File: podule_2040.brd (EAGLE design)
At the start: 100 x 79.8 mm, 58 parts, among them IC1 LT1963EST-3.3, IC2 RP2040-QFN56, IC3 SN74ALVC164245, IC4 SN74ALVC164245, U1 W25Q32FV, Y1 12MHz

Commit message: Schematic & board V1: as used for prototype fab
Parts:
- added C1: 0.1uF, rcl:C0603K
- added R12: 100K, rcl:R0805
- added RESET: Tact sw, SparkFun-Switches:TACTILE_SWITCH_SMD_5.2MM
- GPIO: device SparkFun-Connectors:1X05 -> matt:1X05
- J2: device SparkFun-Connectors:USB-B-MICRO-SMD -> SparkFun-Connectors:USB-MICROB
- LED1: device led:CHIPLED_0805 -> led:CHIPLED_1206
- SWD: device SparkFun-Connectors:1X04 -> matt:1X04
- moved BOOT 8.98 mm to (7.62, 69.8), turned to 90 degrees
- moved BOOTSEL 6.48 mm to (17.8, 74.9), turned to 90 degrees
- moved GPIO 5.08 mm to (62.2, 69.8)
- moved SWD 3.86 mm to (92.7, 49.5)
- moved R3 1.80 mm to (25.4, 67.3)
- moved R11 0.32 mm to (54.3, 73.7)
- moved J2 0.32 mm to (39.7, 78.1), turned to 90 degrees
- turned C12 to 270 degrees
- turned C14 to 270 degrees
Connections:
- removed net N$14: IC2.26, SWD.4
- new net RUN: C1.1, IC2.26, R12.1, RESET.3, SWD.4
- net +3V3: now also R12.2
- net GND: now also C1.2, J2.MT1, J2.MT2, J2.P$1, J2.P$2, RESET.1; no longer J2.SHIELD1, J2.SHIELD2, J2.SHIELD3
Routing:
- net RUN: track 0.00 -> 160.5 mm, vias 0 -> 3
- net N$14: track 43.3 -> 0.00 mm, vias 2 -> 0
- net GND: track 706.3 -> 721.2 mm, vias 43 -> 56
- net +3V3: track 278.9 -> 288.7 mm
- net N$12: track 13.6 -> 21.7 mm
- net +5V: track 173.6 -> 169.8 mm
- net N$11: track 30.2 -> 28.9 mm
- net N$26: track 3.42 -> 4.23 mm
- net N$16: track 44.7 -> 45.3 mm
- net N$15: track 43.2 -> 43.8 mm
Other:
- board text added: "Arc Pipe Podule (c) 2021 Matt Evans v1 31 Aug 2021"
- board text removed: "Arc Pipe Podule (c) 2021 Matt Evans v0.1 23 Aug 2021"

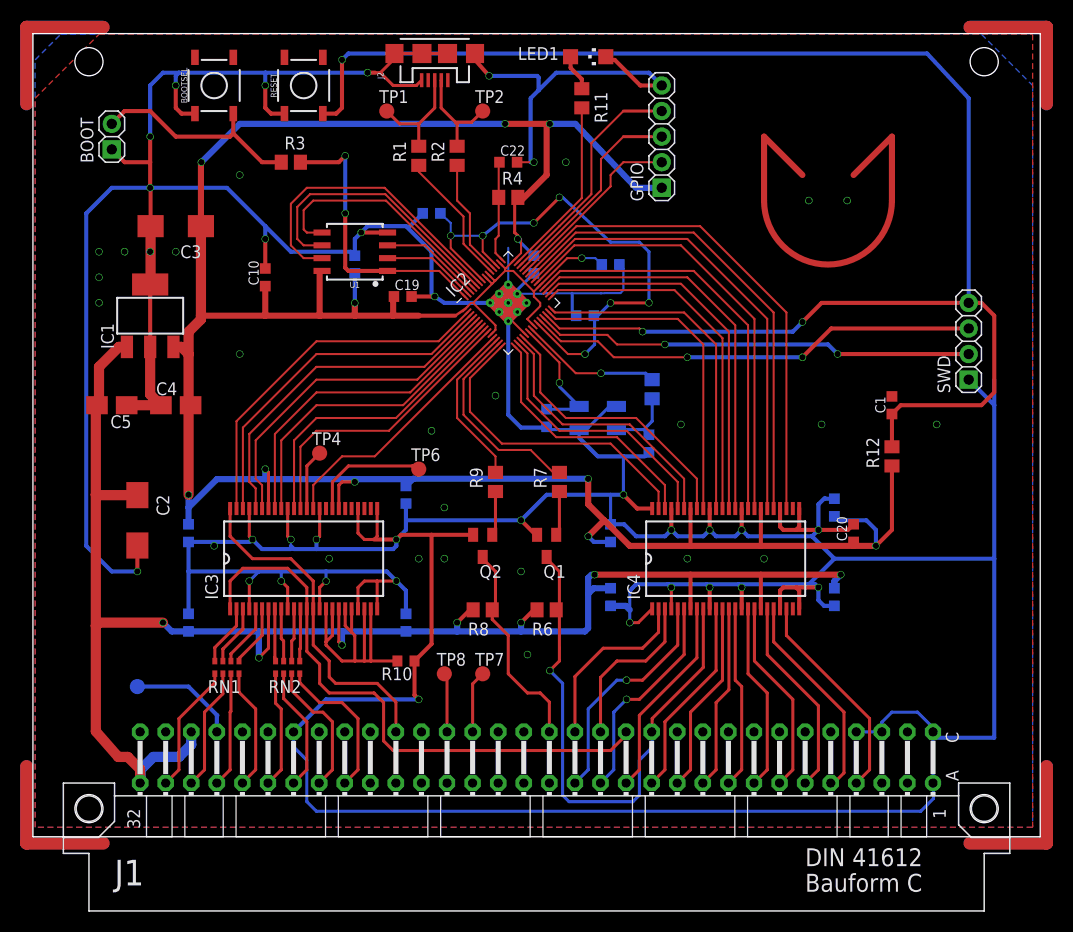
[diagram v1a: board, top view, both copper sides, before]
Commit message: First commit of v2 design, for checking
Changes include:
- Shrink buffers to TSSOP
- Term. resistor packs on internal signals
- Removed N_RST input, freeing 4 GPIOs
- GPIOs to header, prototyping area, and added uSD footprint/resistors
- Moved QSPI closer, more decoupling, re-routed
- Brought reset/boot to a header for remote reboot
- Better labelling/silkscreen tidy, space for serial number
- More common LDO footprint
- Different crystal footprint
- Address lines contiguous
- USB VBUS can power the board, via diodes
- Flash /CS pullup footprint
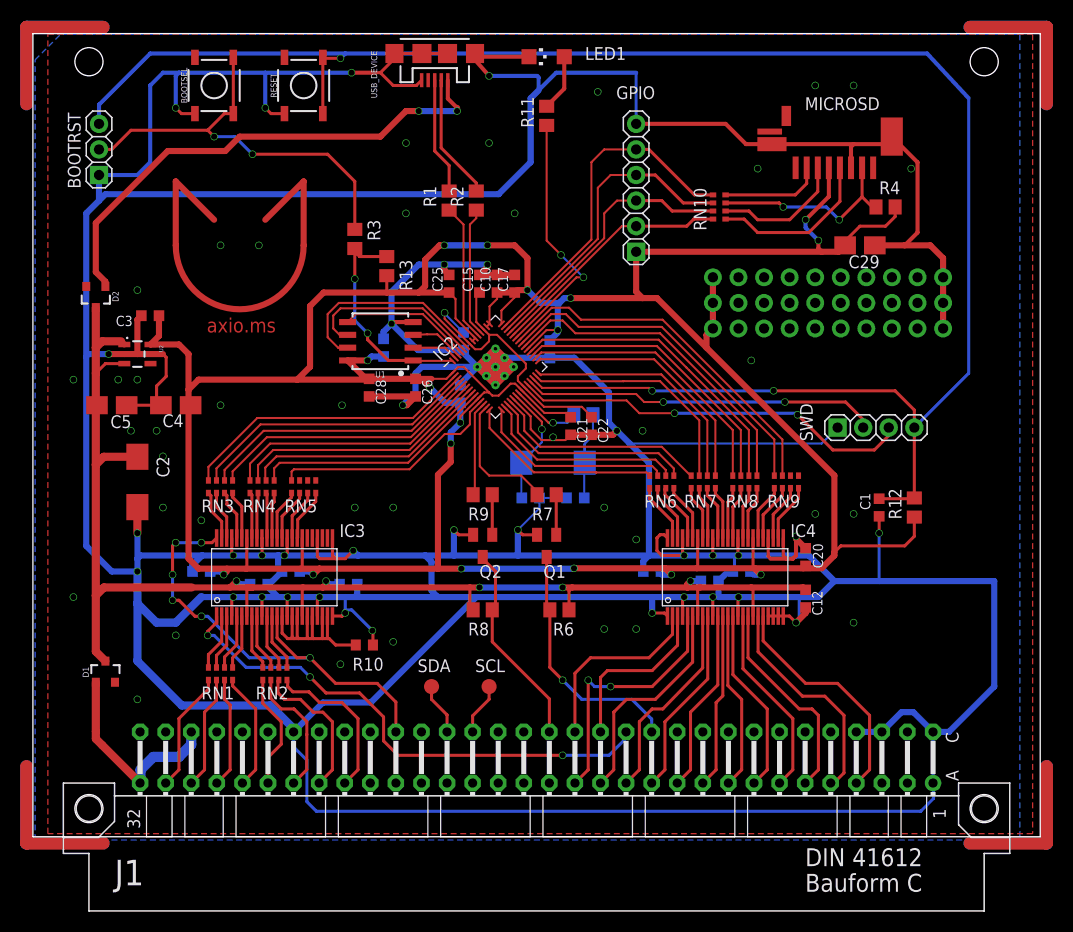
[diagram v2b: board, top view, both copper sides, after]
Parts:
- removed BOOT: (no value), matt:1X02
- removed IC1: LT1963EST-3.3, linear-technology:SOT223
- removed TP1, TP2, TP3, TP4, TP6, TP7, TP8: TPTP15R, testpad:TP15R
- removed Y1: 12MHz, SparkFun-Clocks:CRYSTAL-SMD-5X3.2-4PAD
- added BOOTRST: (no value), matt:1X03
- added C25, C26, C28: 0.1uF, rcl:C0603K
- added C27: 1uF, rcl:C0603K
- added C29: 10uF, rcl:A/3216-18W
- added D1, D2: 700mA/40V/533mV, SparkFun-DiscreteSemi:SOT23-3
- added MICROSD: MOLEX-USD-47309, matt:MOLEX-USD-47309
- added R13: 10K, rcl:R0805
- added RN10: 0, resistor-dil:0603-ARC
- added RN3, RN4, RN5, RN6, RN7, RN8, RN9: 33, resistor-dil:0603-ARC
- added SCL, SDA: TPTP15R, testpad:TP15R
- added U2: 3.3V/150mA, SparkFun-IC-Power:SOT23-5
- added X1: 12MHz, 18pF, IQD-Frequency-Products:7.5X5-2-PAD
- C10: value 0.1uF -> 1uF
- C15: value 2.2uF -> 1uF
- C17, C22: value 2.2uF -> 0.1uF
- C23, C24: value 15pF -> 27pF
- C3: value 100uF -> 1uF; device rcl:CT6032 -> rcl:C0603K
- GPIO: device matt:1X05 -> matt:1X06
- IC3, IC4: value SN74ALVC164245 -> SN74ALVC164245TSSOP48; device matt:DL_R-PDSO-G48 -> matt:TSSOP48
- Q1, Q2: value (none) -> NPN BJT
- R4: value 220 -> 10K
- moved R4 37.5 mm to (84.5, 62.9)
- moved C22 27.5 mm to (55.2, 41.1), turned to 270 degrees
- moved C21 26.8 mm to (53.2, 41.1), flipped to the top, turned to 270 degrees
- moved C10 23.0 mm to (45.9, 55.2)
- moved C6 13.7 mm to (25.4, 26.7), turned to 0 degrees
- moved C16 13.1 mm to (42.5, 49.5), turned to 270 degrees
- moved SWD 12.6 mm to (83.5, 41.0), turned to 0 degrees
- moved C19 11.2 mm to (42.2, 44.3), flipped to the bottom, turned to 90 degrees
- moved C7 11.2 mm to (70.2, 26.7), turned to 0 degrees
- moved C15 10.9 mm to (44.1, 55.2), flipped to the top, turned to 90 degrees
- moved C18 10.4 mm to (51.1, 48.7), turned to 270 degrees
- moved C1 10.2 mm to (83.8, 33.0), turned to 270 degrees
- moved C14 9.97 mm to (67.0, 25.7), turned to 180 degrees
- moved R3 9.92 mm to (31.8, 59.7), turned to 270 degrees
- moved C3 9.25 mm to (11.4, 52.1)
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- renumbered J2 to USB_DEVICE
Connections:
- removed net +12V: J1.C32
- removed net -5V: J1.C2
- removed net N$25: GPIO.4, IC2.40
- removed net NRST_I: IC2.27, IC4.40
- removed net REF8M: J1.C29, TP3.TP
- removed net VBUS: USB_DEVICE.VBUS
- new net +5V/1: D1.1, J1.A32, J1.C30
- new net N$14: MICROSD.2, RN10.8
- new net N$27: IC3.46, RN3.2
- new net N$30: IC3.44, RN3.3
- new net N$31: IC3.43, RN3.4
- new net N$32: IC3.40, RN4.2
- new net N$33: IC3.41, RN4.1
- new net N$34: IC3.38, RN4.3
- new net N$35: IC3.37, RN4.4
- new net N$36: IC3.36, RN5.1
- new net N$37: IC3.35, RN5.2
- new net N$38: IC3.33, RN5.3
- new net N$39: IC4.47, RN6.1
- new net N$40: IC4.46, RN6.2
- new net N$41: IC4.44, RN6.3
- new net N$42: IC4.43, RN6.4
- new net N$43: IC4.41, RN7.1
- new net N$44: IC4.40, RN7.2
- new net N$45: IC4.38, RN7.3
- new net N$46: IC4.37, RN7.4
- new net N$47: IC4.36, RN8.1
- new net N$48: IC4.35, RN8.2
- new net N$49: IC4.33, RN8.3
- new net N$50: IC4.32, RN8.4
- new net N$51: IC4.30, RN9.1
- new net N$52: IC4.29, RN9.2
- new net N$53: IC4.27, RN9.3
- new net N$54: IC4.26, RN9.4
- new net SPI_CS: GPIO.5, IC2.41, RN10.1
- new net SPI_RX: GPIO.4, IC2.40, RN10.2
- new net SPI_SCK: GPIO.2, IC2.38, RN10.4
- new net SPI_TX: GPIO.3, IC2.39, RN10.3
- new net V_USB: D2.1, USB_DEVICE.VBUS
- net +3V3: now also C25.1, C26.1, C27.1, C28.1, C29.+, C3.1, IC2.43, MICROSD.4, R13.2, U2.5; no longer C3.+, IC1.3
- net +5V: now also D1.3, D2.3, U2.1, U2.3; no longer IC1.1, J1.A32, J1.C30
- net A10: now also IC2.32, RN8.6; no longer IC2.34, IC4.32
- net A11: now also IC2.34, RN8.5; no longer IC2.35, IC4.30
- net A12: now also IC2.35, RN9.8; no longer IC2.36, IC4.29
- net A13: now also IC2.36, RN9.7; no longer IC2.37, IC4.27
- net A2: now also RN6.6; no longer IC4.44
- net A3: now also RN6.5; no longer IC4.43
- net A4: now also RN7.8; no longer IC4.41
- net A5: now also IC2.27, RN7.7; no longer IC2.28, IC4.38
- net A6: now also IC2.28, RN7.6; no longer IC2.29, IC4.37
- net A7: now also IC2.29, RN7.5; no longer IC2.30, IC4.36
- net A8: now also IC2.30, RN8.8; no longer IC2.31, IC4.35
- net A9: now also IC2.31, RN8.7; no longer IC2.32, IC4.33
- net D0: now also RN3.8; no longer IC3.47
- net D1: now also RN3.7; no longer IC3.46
- net D2: now also RN3.6; no longer IC3.44
- net D3: now also RN3.5; no longer IC3.43
- net D4: now also RN4.8; no longer IC3.41
- net D5: now also RN4.7; no longer IC3.40
- net D6: now also RN4.6; no longer IC3.38
- net D7: now also RN4.5; no longer IC3.37
- net GND: now also BOOTRST.1, BOOTSEL.2, C25.2, C26.2, C27.2, C28.2, C29.-, C3.2, GPIO.6, IC4.22, IC4.23, MICROSD.6, MICROSD.G1, MICROSD.G2, RESET.2, U2.2; no longer BOOT.1, C3.-, GPIO.5, IC1.2, IC1.4, Y1.2, Y1.4
- net LA10: now also IC4.16; no longer IC4.17
- net LA11: now also IC4.17; no longer IC4.19
- net LA12: now also IC4.19; no longer IC4.20
- net LA13: now also IC4.20; no longer IC4.22
- net LA5: now also IC4.9; no longer IC4.11
- net LA6: now also IC4.11; no longer IC4.12
- net LA7: now also IC4.12; no longer IC4.13
- net LA8: now also IC4.13; no longer IC4.14
- net LA9: now also IC4.14; no longer IC4.16
- net N$10: now also MICROSD.5, RN10.5; no longer C22.1, IC2.43, R4.1
- net N$11: now also R13.1
- net N$12: now also BOOTRST.2, BOOTSEL.4; no longer BOOT.2
- net N$17: now also X1.2; no longer Y1.1
- net N$19: now also X1.1; no longer Y1.3
- net N$21: now also IC3.47, RN3.1; no longer IC3.36, TP4.TP
- net N$22: now also IC3.14
- net N$23: now also MICROSD.3, RN10.6; no longer GPIO.2, IC2.38
- net N$24: now also MICROSD.7, R4.1, RN10.7; no longer GPIO.3, IC2.39
- net N$28: now also IC2.37; no longer IC2.41
- net N$29: now also RN5.4; no longer TP6.TP
- net N$3: no longer TP1.TP
- net N$4: no longer TP2.TP
- net NPS: now also IC3.13; no longer IC3.14
- net NRD: now also RN6.8; no longer IC4.47
- net NRST: no longer IC4.9
- net NSEL: now also RN5.8; no longer IC3.35
- net NWR: now also RN6.7; no longer IC4.46
- net PRNW: no longer IC3.13
- net RUN: now also BOOTRST.3, RESET.4
- net SCL: now also SCL.TP; no longer TP7.TP
- net SDA: now also SDA.TP; no longer TP8.TP
- net VCCINT: now also C22.1
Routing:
- net GND: track 721.2 -> 827.1 mm, vias 56 -> 76
- net +3V3: track 288.7 -> 364.1 mm, vias 12 -> 20
- net V_USB: track 0.00 -> 50.6 mm, vias 0 -> 2
- net SPI_CS: track 0.00 -> 34.4 mm
- net NRST_I: track 33.0 -> 0.00 mm
- net SPI_RX: track 0.00 -> 30.9 mm
- net NRST: track 54.9 -> 24.8 mm
- net +5V: track 169.8 -> 140.7 mm, vias 7 -> 5
- net SPI_TX: track 0.00 -> 27.5 mm
- net VCCINT: track 56.6 -> 30.5 mm, vias 7 -> 1
- net RUN: track 160.5 -> 186.4 mm
- net SPI_SCK: track 0.00 -> 24.7 mm
- net N$25: track 23.4 -> 0.00 mm, vias 0 -> 3
- net +5V/1: track 0.00 -> 20.5 mm
- net N$12: track 21.7 -> 41.9 mm, vias 0 -> 2
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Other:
- board text added: "3.3V"
- board text added: "Arc Pipe Podule (c) 2021 Matt Evans"
- board text added: "Boot"
- board text added: "Gnd"
- board text added: "P26"
- board text added: "P27"
- board text added: "P28"
- board text added: "P29"
- board text added: "Run"
- board text added: "SWCLK"
- board text added: "SWDIO"
- board text added: "axio.ms"
- board text added: "v2 22 Oct 2021"
- board text removed: "Arc Pipe Podule (c) 2021 Matt Evans v1 31 Aug 2021"

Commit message: Tidy-ups for v2
Not released yet: board looks good, work needed on README etc.
Not fabricated yet.
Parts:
- moved C14 0.35 mm to (66.8, 25.4)
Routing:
- net GND: track 827.1 -> 817.8 mm, vias 76 -> 78
- net +5V: track 140.7 -> 141.3 mm
